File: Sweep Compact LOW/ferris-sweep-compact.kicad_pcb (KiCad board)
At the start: 2 copper layers, 107.2 x 86.9 mm, 21 parts, among them J1 MJ-4PP-9, SW10 SW_PUSH, SW11 SW_PUSH, SW12 SW_PUSH, SW14 SW_PUSH, SW15 SW_PUSH, SW16 SW_PUSH, SW17 SW_PUSH, SW18 SW_PUSH, SW2 SW_PUSH, SW20 SW_PUSH, SW21 SW_PUSH, SW3 SW_PUSH, SW4 SW_PUSH, SW5 SW_PUSH, SW6 SW_PUSH, SW8 SW_PUSH, SW9 SW_PUSH, U1 ProMicro

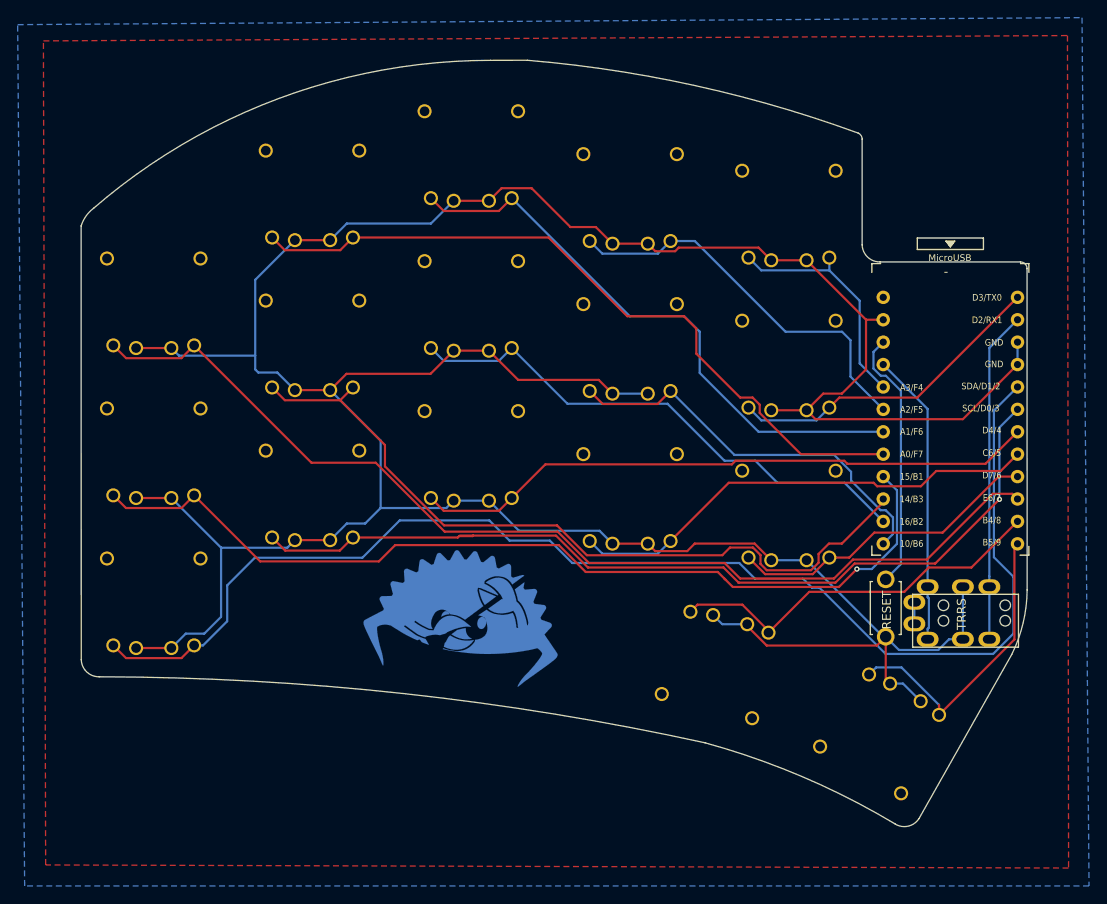
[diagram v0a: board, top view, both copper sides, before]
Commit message: [compact-low]: Fix silk, change reset button, update fills
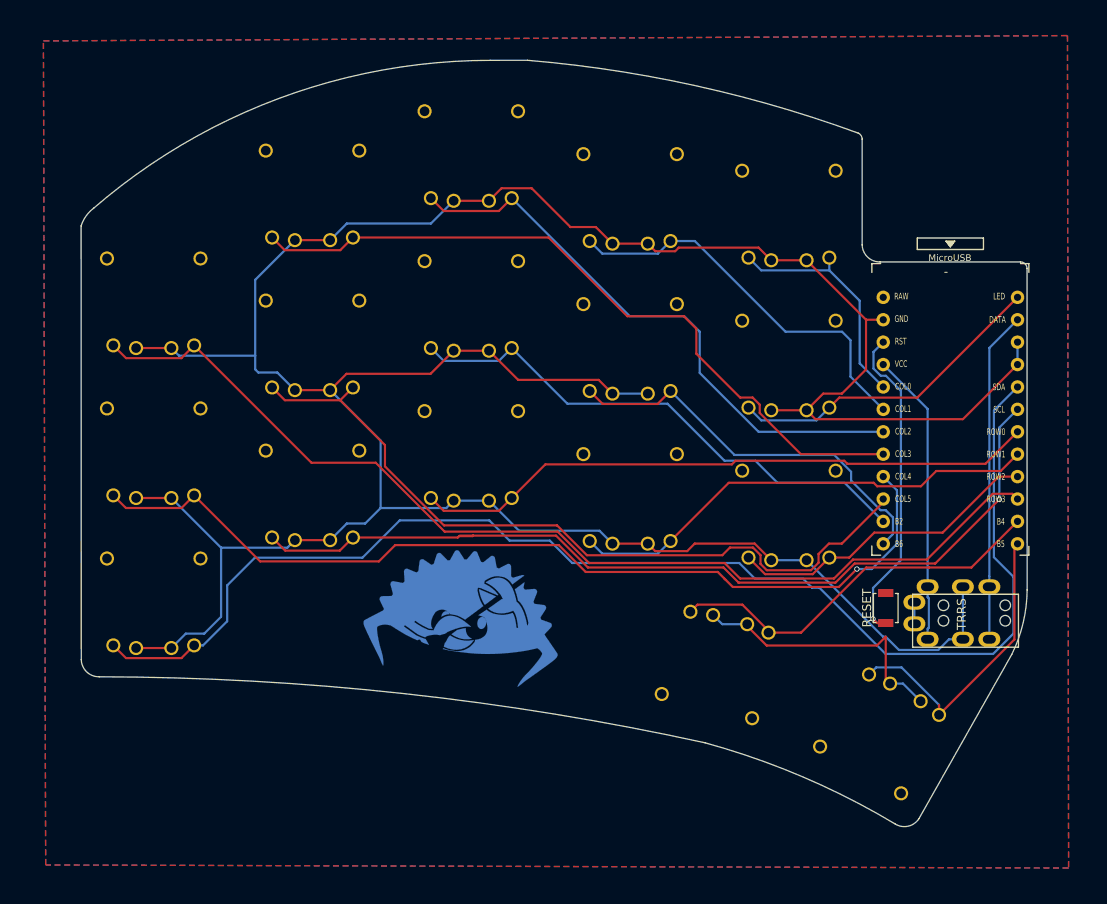
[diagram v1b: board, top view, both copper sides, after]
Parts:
- added RSW1: Val**, * duckyb-collection:SMD_RST_SW [B3U-1000P(M)], B.Cu at (127.0, 77.2)
- RSW1: footprint foostan:ResetSW -> * duckyb-collection:SMD_RST_SW [B3U-1000P(M)]
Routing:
- net reset: track 29.7 -> 38.0 mm, vias 0 -> 1
- added copper zone on B.Cu, net GND
- added copper zone on F.Cu, net GND
- removed copper zone on B.Cu, net (none)
- removed copper zone on F.Cu, net (none)
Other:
- net class Default removed
- board text added: "B2"
- board text added: "B4"
- board text added: "B5"
- board text added: "B6"
- board text added: "COL0"
- board text added: "COL1"
- board text added: "COL2"
- board text added: "COL3"
- board text added: "COL4"
- board text added: "COL5"
- board text added: "DATA"
- board text added: "GND"
- board text added: "LED"
- board text added: "RAW"
- board text added: "ROW0"
- board text added: "ROW1"
- board text added: "ROW2"
- board text added: "ROW3"
- board text added: "RST"
- board text added: "SCL"
- board text added: "SDA"
- board text added: "VCC"
